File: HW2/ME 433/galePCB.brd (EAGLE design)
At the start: 50 x 50 mm, 22 parts, among them J4 USB-MB-H

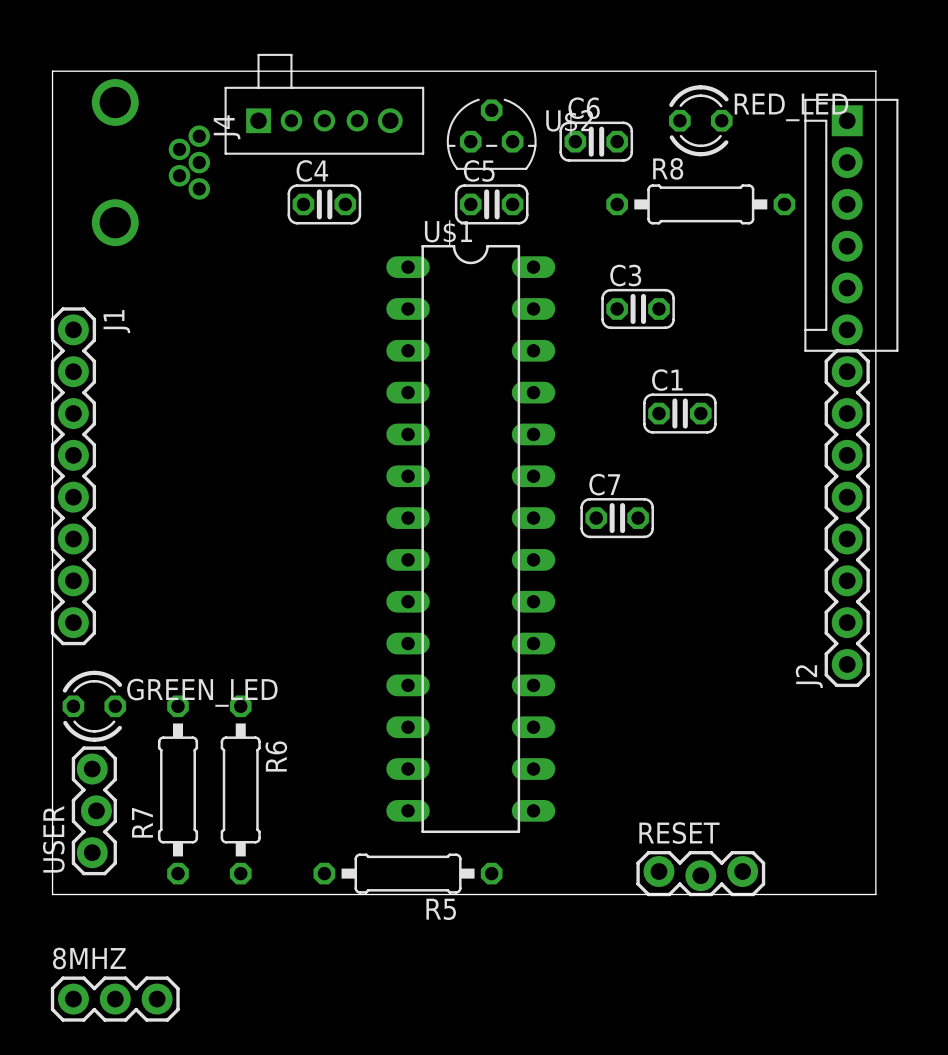
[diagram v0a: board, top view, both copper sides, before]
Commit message: Finished Board positioning
Flipped one of the M08 header pins around to align with given
measurements, changed PICkit to a 5 pin header
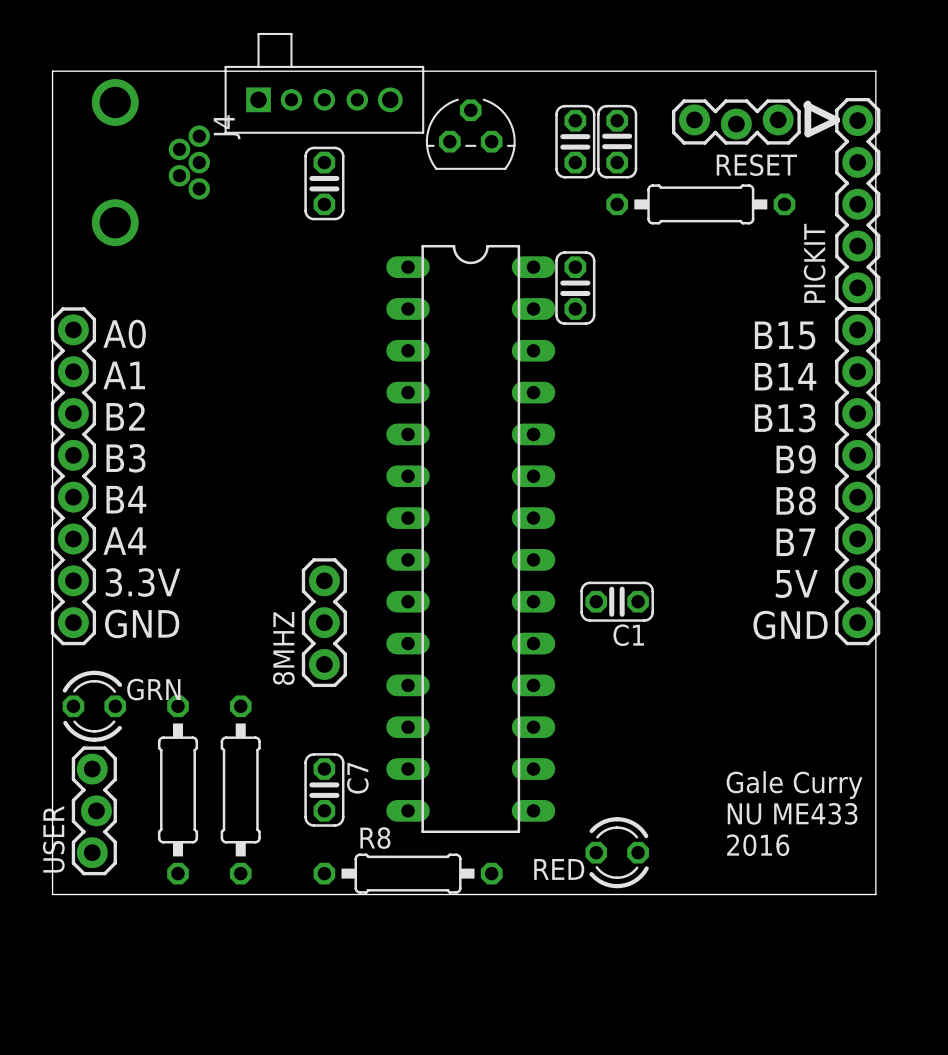
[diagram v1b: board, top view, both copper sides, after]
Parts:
- removed RED_LED: (no value), myPCB:LED3MM
- added RED: (no value), myPCB:LED3MM
- C1: value 10uF -> +10uF-
- C3: value (none) -> 0.1 uF
- PICKIT: device myPCB:MOLEX-1X6 -> myPCB:1X05
- U$1: value PIC32 -> PIC32MX250F128B
- moved RESET 45.7 mm to (39.0, 46.9)
- moved R5 44.4 mm to (39.4, 41.9)
- moved R8 44.4 mm to (21.6, 1.27)
- moved 8MHZ 25.4 mm to (16.5, 14.0), turned to 90 degrees
- moved C7 24.3 mm to (16.5, 6.35), turned to 270 degrees
- moved J1 17.8 mm to (1.27, 16.5), turned to 90 degrees
- moved C1 12.0 mm to (34.3, 17.8), turned to 180 degrees
- moved C5 8.52 mm to (34.3, 45.7), turned to 90 degrees
- moved C3 4.02 mm to (31.8, 36.8), turned to 270 degrees
- moved J2 2.62 mm to (48.9, 16.5)
- moved C4 1.27 mm to (16.5, 43.2), turned to 270 degrees
- moved C6 1.27 mm to (31.8, 45.7), turned to 270 degrees
- moved U$2 1.27 mm to (25.4, 45.7)
- moved U$4 1.27 mm to (16.5, 48.3)
- moved PICKIT 0.64 mm to (48.9, 47.0)
- renumbered GREEN_LED to GRN
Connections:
- net +3V3: now also J1.2, RED.A; no longer J1.7, RED_LED.A
- net A0: now also J1.8; no longer J1.1
- net A1: now also J1.7; no longer J1.2
- net A4/LED: now also J1.3; no longer J1.6
- net B2: now also J1.6; no longer J1.3
- net B3: now also J1.5; no longer J1.4
- net B4/USER: now also J1.4; no longer J1.5
- net GND: now also J1.1; no longer J1.8
- net N$5: now also RED.K; no longer RED_LED.K
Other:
- board text added: "A0 A1 B2 B3 B4 A4 3.3V GND"
- board text added: "B15 B14 B13 B9 B8 B7 5V GND"
- board text added: "Gale Curry NU ME433 2016"

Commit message: Board Fully connected
May need to rotate switch, and need to write pin names on back of board
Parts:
- moved C5 1.27 mm to (35.6, 45.7), turned to 270 degrees
- turned C1 to 0 degrees
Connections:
- removed net N$4: GRN.A, U$1.12
- net A4/LED: now also GRN.A, U$1.12
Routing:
- net B4/USER: track 0.00 -> 32.0 mm
- net B3: track 0.00 -> 21.9 mm
- net B2: track 0.00 -> 21.9 mm
- net A1: track 0.00 -> 20.8 mm
- net A0: track 0.00 -> 20.8 mm
- net N$3: track 0.00 -> 5.61 mm
- net N$2: track 0.00 -> 5.61 mm
- added copper zone on layer 16, net GND
